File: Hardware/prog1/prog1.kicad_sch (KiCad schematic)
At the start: 4 parts, among them J1 Conn_01x02, SW1 SW_Push

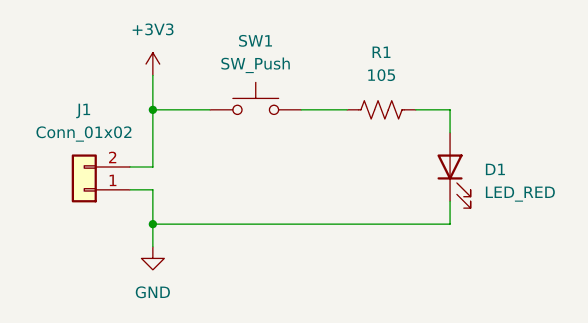
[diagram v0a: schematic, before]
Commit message: rmved template proj files, added power flags, hidden ref. designators on silkscreen layer
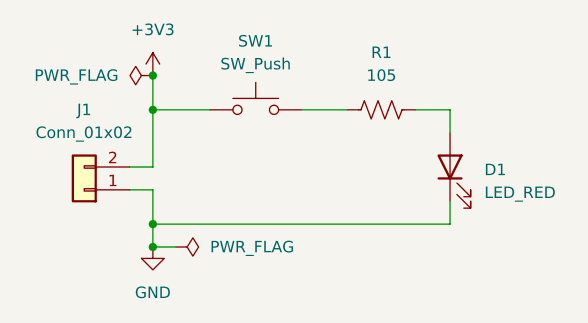
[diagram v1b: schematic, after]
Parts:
- D1: MPN (none) -> LED RED CLEAR 0603 SMD
- R1: MPN (none) -> RES 105 OHM
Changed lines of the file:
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@@
   (junction (at 67.31 86.36) (diameter 0) (color 0 0 0 0)
   )
+  (junction (at 67.31 69.85) (diameter 0) (color 0 0 0 0)
+  )
+  (junction (at 67.31 88.9) (diameter 0) (color 0 0 0 0)
+  )
   (wire (pts (xy 64.77 82.55) (xy 67.31 82.55))
     (stroke (width 0) (type default))
@@
     (stroke (width 0) (type default))
   )
+  (wire (pts (xy 69.85 88.9) (xy 67.31 88.9))
+    (stroke (width 0) (type default))
+  )
   (symbol (lib_id "power:GND") (at 67.31 88.9 0) (unit 1)
     (in_bom yes) (on_board yes) (dnp no) (fields_autoplaced)
@@
       (effects (font (size 1.27 1.27)) hide)
     )
-    (property "MPN" "" (at 92.71 73.66 0)
+    (property "MPN" "RES 105 OHM " (at 92.71 73.66 0)
       (effects (font (size 1.27 1.27)) hide)
     )
@@
       (effects (font (size 1.27 1.27)) hide)
     )
-    (property "MPN" "" (at 100.33 80.01 0)
+    (property "MPN" "LED RED CLEAR 0603 SMD" (at 100.33 80.01 0)
       (effects (font (size 1.27 1.27)) hide)
     )
@@
     )
   )
+  (symbol (lib_id "power:PWR_FLAG") (at 69.85 88.9 270) (unit 1)
+    (in_bom yes) (on_board yes) (dnp no) (fields_autoplaced)
+    (property "Reference" "#FLG02" (at 71.755 88.9 0)
+      (effects (font (size 1.27 1.27)) hide)
+    )
+    (property "Value" "PWR_FLAG" (at 73.66 88.9 90)
+      (effects (font (size 1.27 1.27)) (justify left))
+    )
+    (property "Footprint" "" (at 69.85 88.9 0)
+      (effects (font (size 1.27 1.27)) hide)
+    )
+    (property "Datasheet" "~" (at 69.85 88.9 0)
+      (effects (font (size 1.27 1.27)) hide)
+    )
+    (pin "1")
+    (instances
+      (project "prog1"
+        (path "/1e1b062d-fad0-427c-a622-c5b8a80b5268"
+          (reference "#FLG02") (unit 1)
+        )
+      )
+    )
+  )
   (symbol (lib_id "power:+3V3") (at 67.31 69.85 0) (unit 1)
     (in_bom yes) (on_board yes) (dnp no) (fields_autoplaced)
@@
         )
       )
+    )
+  )
+  (symbol (lib_id "power:PWR_FLAG") (at 67.31 69.85 90) (unit 1)
+    (in_bom yes) (on_board yes) (dnp no) (fields_autoplaced)
+    (property "Reference" "#FLG01" (at 65.405 69.85 0)
+      (effects (font (size 1.27 1.27)) hide)
+    )
+    (property "Value" "PWR_FLAG" (at 63.5 69.85 90)
+      (effects (font (size 1.27 1.27)) (justify left))
+    )
+    (property "Footprint" "" (at 67.31 69.85 0)
+      (effects (font (size 1.27 1.27)) hide)
+    )
+    (property "Datasheet" "~" (at 67.31 69.85 0)
+      (effects (font (size 1.27 1.27)) hide)
+    )
+    (pin "1")
+    (instances
+      (project "prog1"
+        (path "/1e1b062d-fad0-427c-a622-c5b8a80b5268"
+          (reference "#FLG01") (unit 1)
+        )
+      )

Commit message: changed footprint of LED to D_0603
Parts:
- R1: MPN RES 105 OHM -> RES 105 OHM 1/10W 5% AXIAL
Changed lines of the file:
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@@
       (effects (font (size 1.27 1.27)) hide)
     )
-    (property "MPN" "RES 105 OHM " (at 92.71 73.66 0)
+    (property "MPN" "RES 105 OHM 1/10W 5% AXIAL" (at 92.71 73.66 0)
       (effects (font (size 1.27 1.27)) hide)
     )
